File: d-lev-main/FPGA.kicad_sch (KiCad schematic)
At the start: 2 parts, among them J2 Tag-Connect TC2030-NL, U3 AC608

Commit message: many changes to pcb
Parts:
- U3: footprint d-lev:ac608 -> d-lev:ac608-toponly
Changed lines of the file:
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@@
       (effects (font (size 1.27 1.27)))
     )
-    (property "Footprint" "d-lev:ac608" (at 49.53 60.325 0)
+    (property "Footprint" "d-lev:ac608-toponly" (at 49.53 60.325 0)
       (effects (font (size 1.27 1.27)) hide)
     )

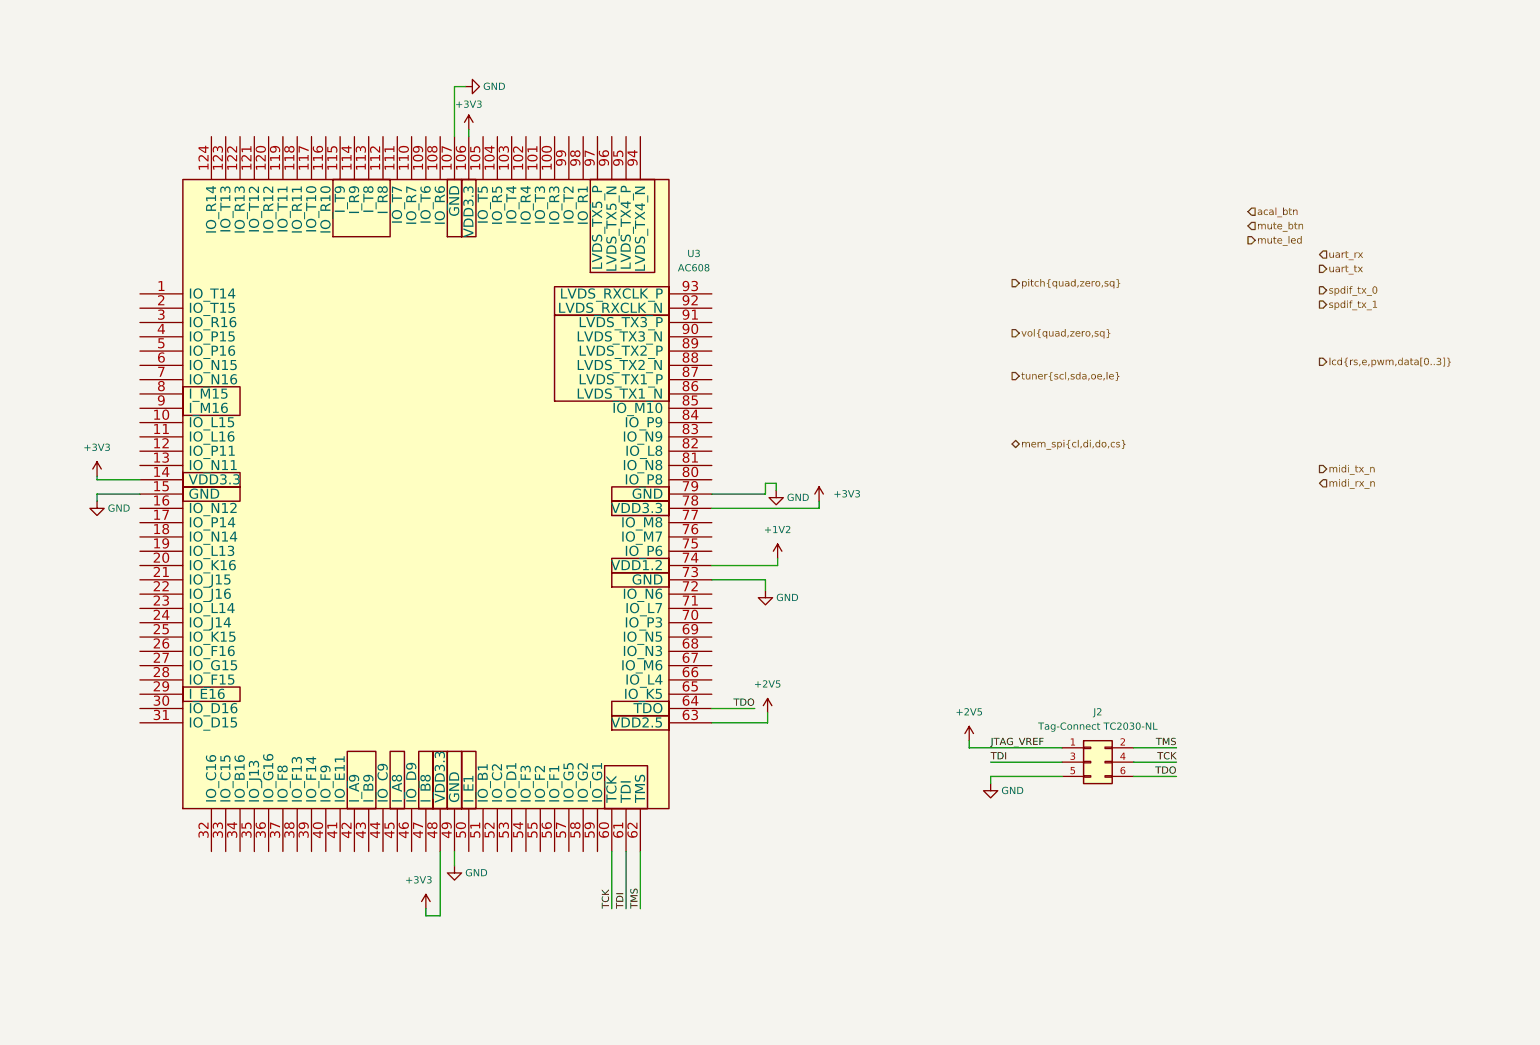
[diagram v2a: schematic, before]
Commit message: Pinned out FPGA and rearranged encoders again
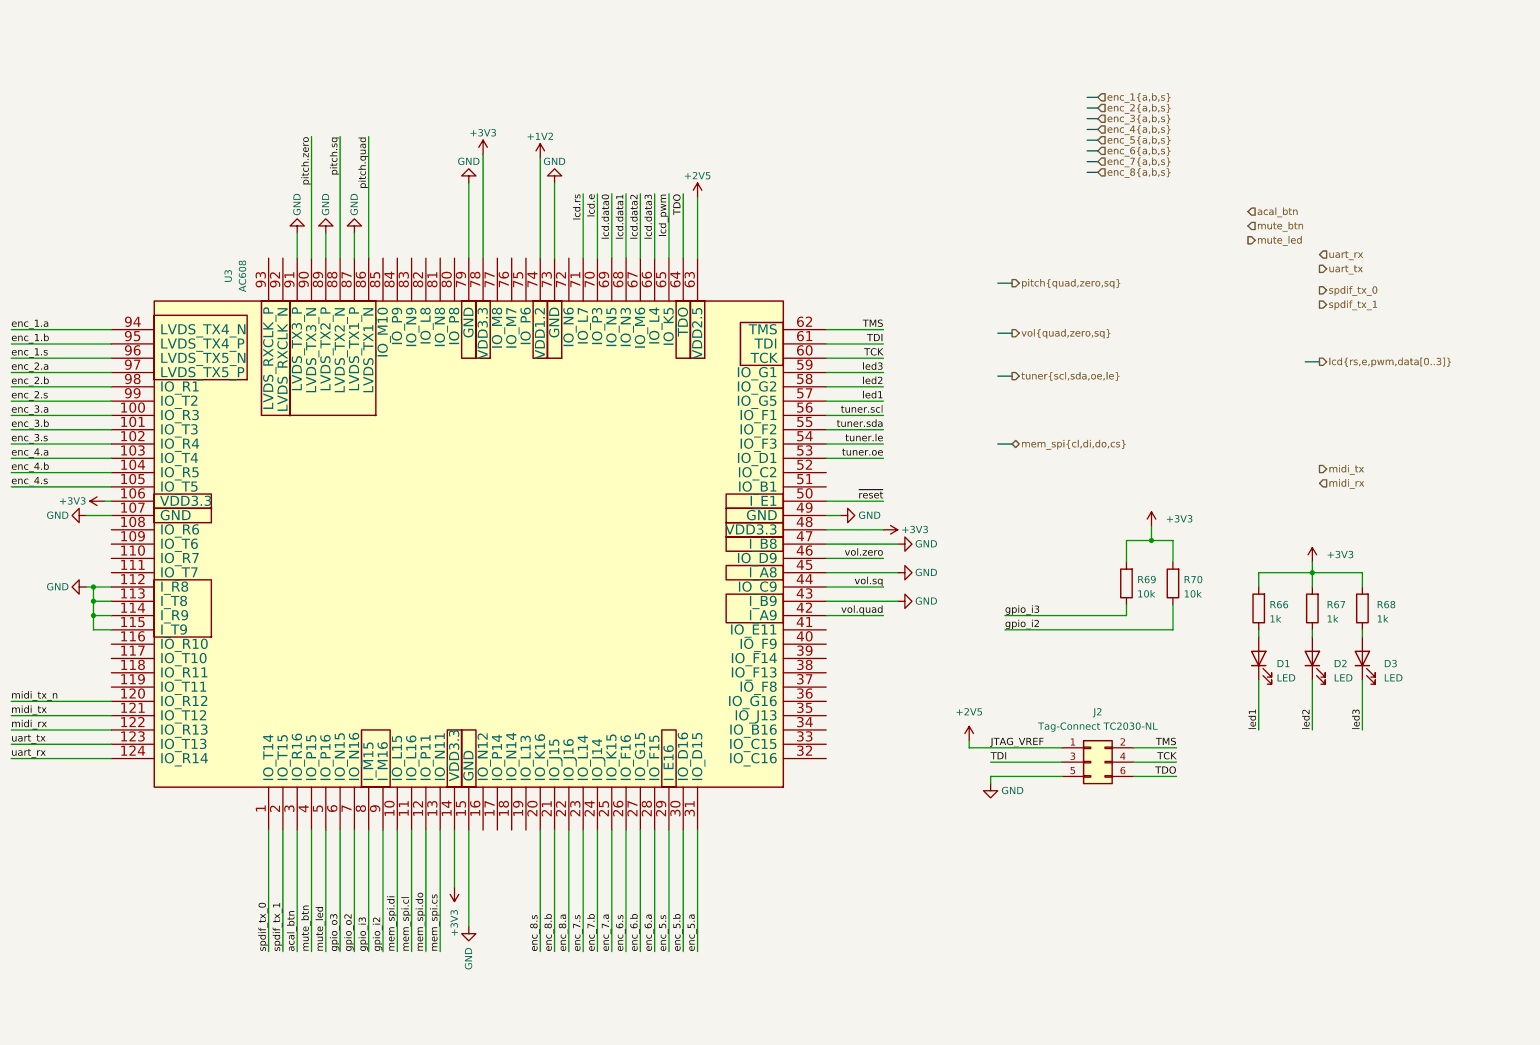
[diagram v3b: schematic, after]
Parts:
- added D1, D2, D3: LED, LED_SMD:LED_0603_1608Metric, symbol Device:LED
- added R66, R67, R68: 1k, Resistor_SMD:R_0603_1608Metric, symbol Device:R
- added R69, R70: 10k, Resistor_SMD:R_0603_1608Metric, symbol Device:R
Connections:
- net +3V3: now also R66.2, R67.2, R68.2, R69.2, R70.2
- net GND: now also U3.112 (I_R8), U3.113 (I_T8), U3.114 (I_R9), U3.115 (I_T9), U3.43 (I_B9), U3.45 (I_A8), U3.47 (I_B8), U3.87 (LVDS_TX1_P), U3.89 (LVDS_TX2_P), U3.91 (LVDS_TX3_P)
- net acal_btn: now also U3.3 (IO_R16)
- net midi_tx_n: now also U3.120 (IO_R12)
- net mute_btn: now also U3.4 (IO_P15)
- net mute_led: now also U3.5 (IO_P16)
- net spdif_tx_0: now also U3.1 (IO_T14)
- net spdif_tx_1: now also U3.2 (IO_T15)
- net uart_rx: now also U3.124 (IO_R14)
- net uart_tx: now also U3.123 (IO_T13)
- net mem_spi.di: now reaches U3.10 (IO_L15)
- net enc_3.a: now reaches U3.100 (IO_R3)
- net enc_3.b: now reaches U3.101 (IO_T3)
- net enc_3.s: now reaches U3.102 (IO_R4)
- net enc_4.a: now reaches U3.103 (IO_T4)
- net enc_4.b: now reaches U3.104 (IO_R5)
- net enc_4.s: now reaches U3.105 (IO_T5)
- net mem_spi.cl: now reaches U3.11 (IO_L16)
- net mem_spi.do: now reaches U3.12 (IO_P11)
- net midi_tx: now reaches U3.121 (IO_T12)
- net midi_rx: now reaches U3.122 (IO_R13)
- net mem_spi.cs: now reaches U3.13 (IO_N11)
- net enc_8.s: now reaches U3.20 (IO_K16)
- net enc_8.b: now reaches U3.21 (IO_J15)
- net enc_8.a: now reaches U3.22 (IO_J16)
- net enc_7.s: now reaches U3.23 (IO_L14)
- net enc_7.b: now reaches U3.24 (IO_J14)
- net enc_7.a: now reaches U3.25 (IO_K15)
- net enc_6.s: now reaches U3.26 (IO_F16)
- net enc_6.b: now reaches U3.27 (IO_G15)
- net enc_6.a: now reaches U3.28 (IO_F15)
- net enc_5.s: now reaches U3.29 (I_E16)
- net enc_5.b: now reaches U3.30 (IO_D16)
- net enc_5.a: now reaches U3.31 (IO_D15)
- net vol.quad: now reaches U3.42 (I_A9)
- net vol.sq: now reaches U3.44 (IO_C9)
- net vol.zero: now reaches U3.46 (IO_D9)
- net ~{reset}: now reaches U3.50 (I_E1)
- net tuner.oe: now reaches U3.53 (IO_D1)
- net tuner.le: now reaches U3.54 (IO_F3)
- net tuner.sda: now reaches U3.55 (IO_F2)
- net tuner.scl: now reaches U3.56 (IO_F1)
- net led1: now reaches U3.57 (IO_G5)
- net led1: now also D1.1 (K)
- net led2: now reaches U3.58 (IO_G2)
- net led2: now also D2.1 (K)
- net led3: now reaches U3.59 (IO_G1)
- net led3: now also D3.1 (K)
- net gpio_o3: now reaches U3.6 (IO_N15)
- net lcd_pwm: now reaches U3.65 (IO_K5)
- net lcd.data3: now reaches U3.66 (IO_L4)
- net lcd.data2: now reaches U3.67 (IO_M6)
- net lcd.data1: now reaches U3.68 (IO_N3)
- net lcd.data0: now reaches U3.69 (IO_N5)
- net gpio_o2: now reaches U3.7 (IO_N16)
- net lcd.e: now reaches U3.70 (IO_P3)
- net lcd.rs: now reaches U3.71 (IO_L7)
- net gpio_i3: now reaches U3.8 (I_M15)
- net gpio_i3: now also R69.1
- net pitch.quad: now reaches U3.86 (LVDS_TX1_N)
- net pitch.sq: now reaches U3.88 (LVDS_TX2_N)
- net gpio_i2: now reaches U3.9 (I_M16)
- net gpio_i2: now also R70.1
- net pitch.zero: now reaches U3.90 (LVDS_TX3_N)
- net enc_1.a: now reaches U3.94 (LVDS_TX4_N)
- net enc_1.b: now reaches U3.95 (LVDS_TX4_P)
- net enc_1.s: now reaches U3.96 (LVDS_TX5_N)
- net enc_2.a: now reaches U3.97 (LVDS_TX5_P)
- net enc_2.b: now reaches U3.98 (IO_R1)
- net enc_2.s: now reaches U3.99 (IO_T2)
- new net: D2.2 (A), R67.1
- new net: D3.2 (A), R68.1
- new net: D1.2 (A), R66.1
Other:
- moved on the sheet: U3

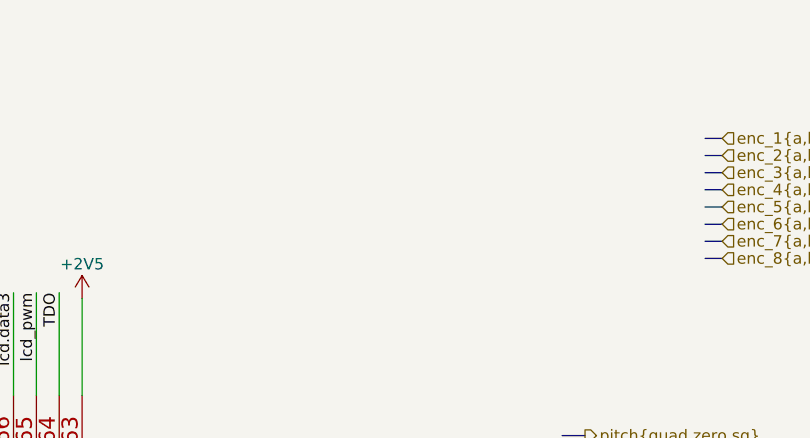
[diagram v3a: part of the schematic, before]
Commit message: Built out power circuitry on d-lev-io
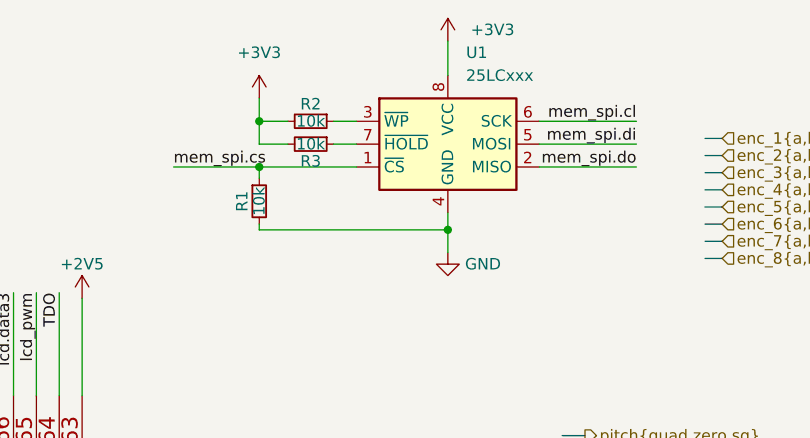
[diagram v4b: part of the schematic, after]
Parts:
- added R1, R2, R3: 10k, Resistor_SMD:R_0603_1608Metric, symbol Device:R_Small
- added U1: 25LCxxx, Package_SO:SOIC-8W_5.3x5.3mm_P1.27mm, symbol Memory_EEPROM:25LCxxx
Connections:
- net +3V3: now also R2.2, R3.2, U1.8 (VCC)
- net GND: now also R1.2, U1.4 (GND)
- net mem_spi.cl: now also U1.6 (SCK)
- net mem_spi.cs: now also R1.1, U1.1 (~{CS})
- net mem_spi.di: now also U1.5 (MOSI)
- net mem_spi.do: now also U1.2 (MISO)
- new net: R2.1, U1.3 (~{WP})
- new net: R3.1, U1.7 (~{HOLD})
